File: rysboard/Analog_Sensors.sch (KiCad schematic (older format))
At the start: 25 parts, among them J14 BAT2_TH, J21 BAT3_TH, J22 BAT2_TH, J23 BAT2_TH, J8 BAT1_TH, Q10 DMP2075UFDB

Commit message: pre cleanup
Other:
- moved on the sheet: R52, R53, R55, R56, R57, TH2
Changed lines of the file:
@@
 $Descr A4 11693 8268
 encoding utf-8
-Sheet 6 7
+Sheet 5 7
 Title ""
 Date ""
@@
 Text HLabel 4100 1300 0    50   Input ~ 0
 BAT_T_3
-Text HLabel 2500 2525 0    50   Input ~ 0
+Text HLabel 3150 2875 0    50   Input ~ 0
 BOARD_T_1
 Text HLabel 6150 1275 0    50   Input ~ 0
 CHASSIS_T_2
-Text HLabel 1700 4550 0    50   Input ~ 0
+Text HLabel 2425 4375 0    50   Input ~ 0
 V_P_20
-Text HLabel 2850 4550 0    50   Input ~ 0
+Text HLabel 3575 4375 0    50   Input ~ 0
 V_P_5
 Text HLabel 1600 5650 0    50   Input ~ 0
@@
 $EndComp
 Wire Wire Line
-	2500 2175 2500 2225
+	3150 2525 3150 2575
 $Comp
 L power:GND #PWR049
 U 1 1 603EF9F9
-P 2100 2925
-F 0 "#PWR049" H 2100 2675 50  0001 C CNN
-F 1 "GND" H 2105 2752 50  0000 C CNN
-F 2 "" H 2100 2925 50  0001 C CNN
-F 3 "" H 2100 2925 50  0001 C CNN
-	1    2100 2925
+P 2750 3275
+F 0 "#PWR049" H 2750 3025 50  0001 C CNN
+F 1 "GND" H 2755 3102 50  0000 C CNN
+F 2 "" H 2750 3275 50  0001 C CNN
+F 3 "" H 2750 3275 50  0001 C CNN
+	1    2750 3275
 	-1   0    0    -1
 $EndComp
@@
 L Device:Thermistor_PTC TH2
 U 1 1 603F0105
-P 2500 2675
-F 0 "TH2" H 2598 2721 50  0000 L CNN
-F 1 "Thermistor_PTC" H 2598 2630 50  0000 L CNN
-F 2 "Resistor_SMD:R_0805_2012Metric_Pad1.15x1.40mm_HandSolder" H 2550 2475 50  0001 L CNN
-F 3 "~" H 2500 2675 50  0001 C CNN
-	1    2500 2675
-	1    0    0    -1
-$EndComp
-Wire Wire Line
-	2100 2825 2100 2925
-Wire Wire Line
-	2500 2825 2100 2825
+P 3150 3025
+F 0 "TH2" H 3248 3071 50  0000 L CNN
+F 1 "Thermistor_PTC" H 3248 2980 50  0000 L CNN
+F 2 "Resistor_SMD:R_0805_2012Metric_Pad1.15x1.40mm_HandSolder" H 3200 2825 50  0001 L CNN
+F 3 "~" H 3150 3025 50  0001 C CNN
+	1    3150 3025
+	1    0    0    -1
+$EndComp
+Wire Wire Line
+	2750 3175 2750 3275
+Wire Wire Line
+	3150 3175 2750 3175
 $Comp
 L power:+24V #PWR026
 U 1 1 603F23C7
-P 2050 4250
-F 0 "#PWR026" H 2050 4100 50  0001 C CNN
-F 1 "+24V" H 2065 4423 50  0000 C CNN
-F 2 "" H 2050 4250 50  0001 C CNN
-F 3 "" H 2050 4250 50  0001 C CNN
-	1    2050 4250
+P 2775 4075
+F 0 "#PWR026" H 2775 3925 50  0001 C CNN
+F 1 "+24V" H 2790 4248 50  0000 C CNN
+F 2 "" H 2775 4075 50  0001 C CNN
+F 3 "" H 2775 4075 50  0001 C CNN
+	1    2775 4075
 	1    0    0    -1
 $EndComp
@@
 L power:+5V #PWR051
 U 1 1 603F2BD7
-P 3150 4250
-F 0 "#PWR051" H 3150 4100 50  0001 C CNN
-F 1 "+5V" H 3165 4423 50  0000 C CNN
-F 2 "" H 3150 4250 50  0001 C CNN
-F 3 "" H 3150 4250 50  0001 C CNN
-	1    3150 4250
-	1    0    0    -1
-$EndComp
-Wire Wire Line
-	3150 4550 2850 4550
+P 3875 4075
+F 0 "#PWR051" H 3875 3925 50  0001 C CNN
+F 1 "+5V" H 3890 4248 50  0000 C CNN
+F 2 "" H 3875 4075 50  0001 C CNN
+F 3 "" H 3875 4075 50  0001 C CNN
+	1    3875 4075
+	1    0    0    -1
+$EndComp
+Wire Wire Line
+	3875 4375 3575 4375
 Text GLabel 2050 5650 2    50   Output ~ 0
 Bat_Current_Pos
@@
 L Device:R R52
 U 1 1 60405D8A
-P 2050 4400
-F 0 "R52" H 2120 4446 50  0000 L CNN
-F 1 "9KR0.5%" H 2120 4355 50  0000 L CNN
-F 2 "Resistor_SMD:R_0603_1608Metric" V 1980 4400 50  0001 C CNN
-F 3 "~" H 2050 4400 50  0001 C CNN
-	1    2050 4400
+P 2775 4225
+F 0 "R52" H 2845 4271 50  0000 L CNN
+F 1 "9KR0.5%" H 2845 4180 50  0000 L CNN
+F 2 "Resistor_SMD:R_0603_1608Metric" V 2705 4225 50  0001 C CNN
+F 3 "~" H 2775 4225 50  0001 C CNN
+	1    2775 4225
 	1    0    0    -1
 $EndComp
@@
 L Device:R R53
 U 1 1 60406110
-P 2050 4700
-F 0 "R53" H 1980 4654 50  0000 R CNN
-F 1 "1KR0.5%" H 1980 4745 50  0000 R CNN
-F 2 "Resistor_SMD:R_0603_1608Metric" V 1980 4700 50  0001 C CNN
-F 3 "~" H 2050 4700 50  0001 C CNN
-	1    2050 4700
+P 2775 4525
+F 0 "R53" H 2705 4479 50  0000 R CNN
+F 1 "1KR0.5%" H 2705 4570 50  0000 R CNN
+F 2 "Resistor_SMD:R_0603_1608Metric" V 2705 4525 50  0001 C CNN
+F 3 "~" H 2775 4525 50  0001 C CNN
+	1    2775 4525
 	-1   0    0    1
 $EndComp
@@
 L power:GND #PWR028
 U 1 1 6040647E
-P 2050 4850
-F 0 "#PWR028" H 2050 4600 50  0001 C CNN
-F 1 "GND" H 2055 4677 50  0000 C CNN
-F 2 "" H 2050 4850 50  0001 C CNN
-F 3 "" H 2050 4850 50  0001 C CNN
-	1    2050 4850
+P 2775 4675
+F 0 "#PWR028" H 2775 4425 50  0001 C CNN
+F 1 "GND" H 2780 4502 50  0000 C CNN
+F 2 "" H 2775 4675 50  0001 C CNN
+F 3 "" H 2775 4675 50  0001 C CNN
+	1    2775 4675
 	-1   0    0    -1
 $EndComp
 Wire Wire Line
-	1700 4550 2050 4550
-Connection ~ 2050 4550
+	2425 4375 2775 4375
+Connection ~ 2775 4375
 $Comp
 L power:GND #PWR052
 U 1 1 604093E1
-P 3150 4850
-F 0 "#PWR052" H 3150 4600 50  0001 C CNN
-F 1 "GND" H 3155 4677 50  0000 C CNN
-F 2 "" H 3150 4850 50  0001 C CNN
-F 3 "" H 3150 4850 50  0001 C CNN
-	1    3150 4850
+P 3875 4675
+F 0 "#PWR052" H 3875 4425 50  0001 C CNN
+F 1 "GND" H 3880 4502 50  0000 C CNN
+F 2 "" H 3875 4675 50  0001 C CNN
+F 3 "" H 3875 4675 50  0001 C CNN
+	1    3875 4675
 	-1   0    0    -1
 $EndComp
-Text Notes 3950 4850 0    50   ~ 0
+Text Notes 4675 4675 0    50   ~ 0
 33v == 3.3v\n\nR=U/I\nI=U/R1+R2\nR1 =90KOhm\nR2 = 10KOhm\n\n9.9 == 3.3V\nR1 = 10KOhm\nR2 =  5KOhm
-Text Notes 3900 3900 0    50   ~ 0
+Text Notes 4625 3725 0    50   ~ 0
 TO DO:\nDouble check values\n
 $Comp
@@
 L Device:R R56
 U 1 1 603B9257
-P 3150 4400
-F 0 "R56" H 3220 4446 50  0000 L CNN
-F 1 "10KR" H 3220 4355 50  0000 L CNN
-F 2 "Resistor_SMD:R_0603_1608Metric" V 3080 4400 50  0001 C CNN
-F 3 "~" H 3150 4400 50  0001 C CNN
-	1    3150 4400
+P 3875 4225
+F 0 "R56" H 3945 4271 50  0000 L CNN
+F 1 "10KR" H 3945 4180 50  0000 L CNN
+F 2 "Resistor_SMD:R_0603_1608Metric" V 3805 4225 50  0001 C CNN
+F 3 "~" H 3875 4225 50  0001 C CNN
+	1    3875 4225
 	1    0    0    -1
 $EndComp
@@
 L Device:R R57
 U 1 1 603B976E
-P 3150 4700
-F 0 "R57" H 3220 4746 50  0000 L CNN
-F 1 "5KR" H 3220 4655 50  0000 L CNN
-F 2 "Resistor_SMD:R_0603_1608Metric" V 3080 4700 50  0001 C CNN
-F 3 "~" H 3150 4700 50  0001 C CNN
-	1    3150 4700
-	1    0    0    -1
-$EndComp
-Connection ~ 3150 4550
+P 3875 4525
+F 0 "R57" H 3945 4571 50  0000 L CNN
+F 1 "5KR" H 3945 4480 50  0000 L CNN
+F 2 "Resistor_SMD:R_0603_1608Metric" V 3805 4525 50  0001 C CNN
+F 3 "~" H 3875 4525 50  0001 C CNN
+	1    3875 4525
+	1    0    0    -1
+$EndComp
+Connection ~ 3875 4375
 Text GLabel 8625 1800 1    50   Output ~ 0
 MCU_3.3V
@@
 L Device:R R55
 U 1 1 603BD637
-P 2500 2375
-F 0 "R55" H 2570 2421 50  0000 L CNN
-F 1 "10KR" H 2570 2330 50  0000 L CNN
-F 2 "Resistor_SMD:R_0603_1608Metric" V 2430 2375 50  0001 C CNN
-F 3 "~" H 2500 2375 50  0001 C CNN
-	1    2500 2375
+P 3150 2725
+F 0 "R55" H 3220 2771 50  0000 L CNN
+F 1 "10KR" H 3220 2680 50  0000 L CNN
+F 2 "Resistor_SMD:R_0603_1608Metric" V 3080 2725 50  0001 C CNN
+F 3 "~" H 3150 2725 50  0001 C CNN
+	1    3150 2725
 	1    0    0    -1
 $EndComp
@@
 Wire Wire Line
 	5250 750  5250 900
-Text GLabel 2500 2175 0    50   Input ~ 0
+Text GLabel 3150 2525 0    50   Input ~ 0
 MCU_ANALOG_SENSOR_V
 $EndSCHEMATC

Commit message: cleanup and energy managment scheeme started
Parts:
- removed J14: BAT2_TH, symbol Connector_Generic:Conn_01x02
- removed J21: BAT3_TH, symbol Connector_Generic:Conn_01x02
- removed J8: BAT1_TH, symbol Connector_Generic:Conn_01x02
- removed R54, R58, R60: 10KR, Resistor_SMD:R_0603_1608Metric, symbol Device:R
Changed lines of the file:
@@
 Comment4 ""
 $EndDescr
-Text HLabel 3325 1300 0    50   Input ~ 0
-BAT_T_2
-Text HLabel 4100 1300 0    50   Input ~ 0
-BAT_T_3
 Text HLabel 3150 2875 0    50   Input ~ 0
 BOARD_T_1
@@
 Text HLabel 7850 4550 0    50   Input ~ 0
 V_BAT_C3
-$Comp
-L Connector_Generic:Conn_01x02 J8
-U 1 1 603EB5C9
-P 2500 1550
-F 0 "J8" V 2372 1630 50  0000 L CNN
-F 1 "BAT1_TH" V 2463 1630 50  0000 L CNN
-F 2 "" H 2500 1550 50  0001 C CNN
-F 3 "~" H 2500 1550 50  0001 C CNN
-	1    2500 1550
-	0    1    1    0
-$EndComp
-$Comp
-L Connector_Generic:Conn_01x02 J14
-U 1 1 603EBF1A
-P 3475 1550
-F 0 "J14" V 3347 1630 50  0000 L CNN
-F 1 "BAT2_TH" V 3438 1630 50  0000 L CNN
-F 2 "" H 3475 1550 50  0001 C CNN
-F 3 "~" H 3475 1550 50  0001 C CNN
-	1    3475 1550
-	0    1    1    0
-$EndComp
-$Comp
-L Connector_Generic:Conn_01x02 J21
-U 1 1 603EC2EC
-P 4250 1550
-F 0 "J21" V 4122 1630 50  0000 L CNN
-F 1 "BAT3_TH" V 4213 1630 50  0000 L CNN
-F 2 "" H 4250 1550 50  0001 C CNN
-F 3 "~" H 4250 1550 50  0001 C CNN
-	1    4250 1550
-	0    1    1    0
-$EndComp
-$Comp
-L power:GND #PWR050
-U 1 1 603ED9D9
-P 2500 1350
-F 0 "#PWR050" H 2500 1100 50  0001 C CNN
-F 1 "GND" H 2505 1177 50  0000 C CNN
-F 2 "" H 2500 1350 50  0001 C CNN
-F 3 "" H 2500 1350 50  0001 C CNN
-	1    2500 1350
-	0    -1   1    0
-$EndComp
-$Comp
-L power:GND #PWR053
-U 1 1 603EDE43
-P 3475 1350
-F 0 "#PWR053" H 3475 1100 50  0001 C CNN
-F 1 "GND" H 3480 1177 50  0000 C CNN
-F 2 "" H 3475 1350 50  0001 C CNN
-F 3 "" H 3475 1350 50  0001 C CNN
-	1    3475 1350
-	0    -1   -1   0
-$EndComp
-$Comp
-L power:GND #PWR054
-U 1 1 603EE031
-P 4250 1350
-F 0 "#PWR054" H 4250 1100 50  0001 C CNN
-F 1 "GND" H 4255 1177 50  0000 C CNN
-F 2 "" H 4250 1350 50  0001 C CNN
-F 3 "" H 4250 1350 50  0001 C CNN
-	1    4250 1350
-	0    -1   -1   0
-$EndComp
 Wire Wire Line
 	3150 2525 3150 2575
@@
 Text Notes 7750 3650 0    50   ~ 0
 0-15.086V\n
-Text HLabel 2350 1300 0    50   Input ~ 0
-BAT_T_1
-Wire Wire Line
-	2350 1300 2400 1300
-Wire Wire Line
-	2400 1300 2400 1350
-Wire Wire Line
-	2400 1300 2400 1250
-Connection ~ 2400 1300
-Wire Wire Line
-	3325 1300 3375 1300
-Wire Wire Line
-	3375 1300 3375 1250
-Wire Wire Line
-	3375 1300 3375 1350
-Connection ~ 3375 1300
-Wire Wire Line
-	4100 1300 4150 1300
-Wire Wire Line
-	4150 1300 4150 1250
-Wire Wire Line
-	4150 1300 4150 1350
-Connection ~ 4150 1300
 $Comp
 L Device:R R70
@@
 Text GLabel 8625 1800 1    50   Output ~ 0
 MCU_3.3V
-Wire Wire Line
-	2400 900  2400 950
-Wire Wire Line
-	4150 900  4150 950
 $Comp
 L Device:R R55
@@
 When not used, thermistors do not need to be powered on.
 $Comp
-L Device:R R54
-U 1 1 603FD549
-P 2400 1100
-F 0 "R54" H 2470 1146 50  0000 L CNN
-F 1 "10KR" H 2470 1055 50  0000 L CNN
-F 2 "Resistor_SMD:R_0603_1608Metric" V 2330 1100 50  0001 C CNN
-F 3 "~" H 2400 1100 50  0001 C CNN
-	1    2400 1100
-	1    0    0    -1
-$EndComp
-$Comp
-L Device:R R58
-U 1 1 603FD808
-P 3375 1100
-F 0 "R58" H 3445 1146 50  0000 L CNN
-F 1 "10KR" H 3445 1055 50  0000 L CNN
-F 2 "Resistor_SMD:R_0603_1608Metric" V 3305 1100 50  0001 C CNN
-F 3 "~" H 3375 1100 50  0001 C CNN
-	1    3375 1100
-	1    0    0    -1
-$EndComp
-$Comp
-L Device:R R60
-U 1 1 603FDA2E
-P 4150 1100
-F 0 "R60" H 4220 1146 50  0000 L CNN
-F 1 "10KR" H 4220 1055 50  0000 L CNN
-F 2 "Resistor_SMD:R_0603_1608Metric" V 4080 1100 50  0001 C CNN
-F 3 "~" H 4150 1100 50  0001 C CNN
-	1    4150 1100
-	1    0    0    -1
-$EndComp
-$Comp
 L rysboard:DMP2075UFDB Q10
 U 1 1 605EDFDE
@@
 Wire Wire Line
 	6150 1225 6150 1375
-Text HLabel 5250 1275 0    50   Input ~ 0
-CHASSIS_T_1
 Wire Wire Line
 	5250 1200 5250 1350
@@
 Text GLabel 5250 750  2    50   Input ~ 0
 MCU_ANALOG_SENSOR_V
-Text GLabel 4150 900  2    50   Input ~ 0
-MCU_ANALOG_SENSOR_V
-Text GLabel 3375 750  2    50   Input ~ 0
-MCU_ANALOG_SENSOR_V
-Wire Wire Line
-	3375 750  3375 950
-Text GLabel 2400 900  2    50   Input ~ 0
-MCU_ANALOG_SENSOR_V
 Wire Wire Line
 	5250 750  5250 900
 Text GLabel 3150 2525 0    50   Input ~ 0
 MCU_ANALOG_SENSOR_V
+Text HLabel 5250 1275 0    50   Input ~ 0
+CHASSIS_T_1
 $EndSCHEMATC

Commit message: started board project
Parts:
- J22: value BAT2_TH -> CH1_T; footprint (none) -> Connector_PinHeader_2.54mm:PinHeader_1x02_P2.54mm_Vertical
- J23: value BAT2_TH -> CH2_T; footprint (none) -> Connector_PinHeader_2.54mm:PinHeader_1x02_P2.54mm_Vertical
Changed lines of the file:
@@
 P 6250 1575
 F 0 "J23" V 6122 1655 50  0000 L CNN
-F 1 "BAT2_TH" V 6213 1655 50  0000 L CNN
-F 2 "" H 6250 1575 50  0001 C CNN
+F 1 "CH2_T" V 6213 1655 50  0000 L CNN
+F 2 "Connector_PinHeader_2.54mm:PinHeader_1x02_P2.54mm_Vertical" H 6250 1575 50  0001 C CNN
 F 3 "~" H 6250 1575 50  0001 C CNN
 	1    6250 1575
@@
 P 5350 1550
 F 0 "J22" V 5222 1630 50  0000 L CNN
-F 1 "BAT2_TH" V 5313 1630 50  0000 L CNN
-F 2 "" H 5350 1550 50  0001 C CNN
+F 1 "CH1_T" V 5313 1630 50  0000 L CNN
+F 2 "Connector_PinHeader_2.54mm:PinHeader_1x02_P2.54mm_Vertical" H 5350 1550 50  0001 C CNN
 F 3 "~" H 5350 1550 50  0001 C CNN
 	1    5350 1550

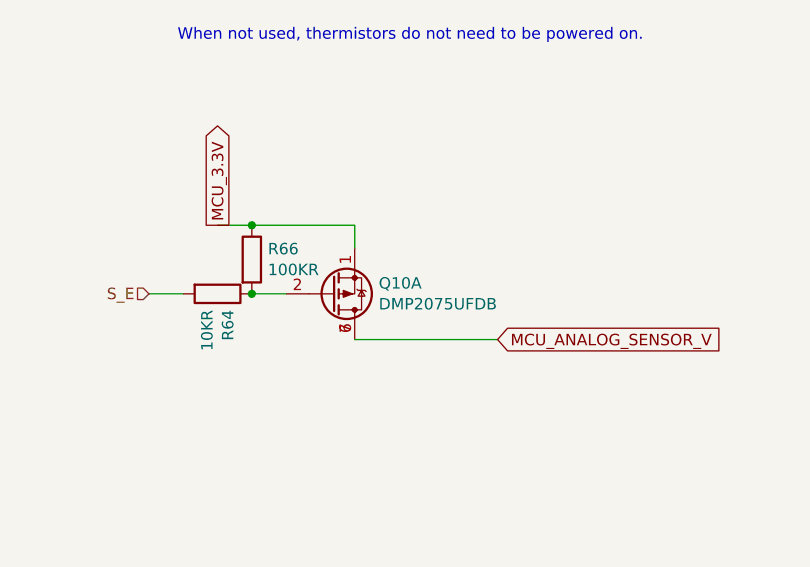
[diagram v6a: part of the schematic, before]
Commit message: st motor drivers done
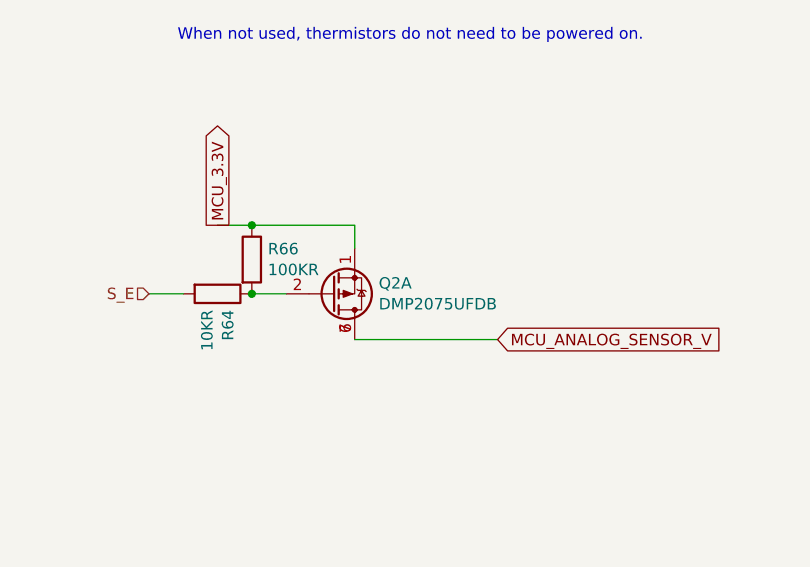
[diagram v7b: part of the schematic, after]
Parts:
- renumbered Q10 to Q2
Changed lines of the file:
@@
 When not used, thermistors do not need to be powered on.
 $Comp
-L rysboard:DMP2075UFDB Q10
+L rysboard:DMP2075UFDB Q2
 U 1 1 605EDFDE
 P 9125 2100
-F 0 "Q10" H 9330 2054 50  0000 L CNN
+F 0 "Q2" H 9330 2054 50  0000 L CNN
 F 1 "DMP2075UFDB" H 9330 2145 50  0000 L CNN
 F 2 "SamacSys_Parts:DMP2075UFDB7" H 9325 2025 50  0001 L CIN

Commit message: stm scheeme
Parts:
- added R?: 10KR, Resistor_SMD:R_0603_1608Metric, symbol Device:R
- added TH?: Thermistor_PTC, Resistor_SMD:R_0805_2012Metric_Pad1.15x1.40mm_HandSolder, symbol Device:Thermistor_PTC
- J22, J23: footprint Connector_PinHeader_2.54mm:PinHeader_1x02_P2.54mm_Vertical -> Connector_PinHeader_1.00mm:PinHeader_1x02_P1.00mm_Vertical
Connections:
- net GND: now also TH?.2
- net MCU_ANALOG_SENSOR_V: now also R?.1
- new net: R?.2, TH?.1
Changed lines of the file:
@@
 0-15.086V\n
-$Comp
-L Device:R R70
-U 1 1 603B8902
-P 7050 4400
-F 0 "R70" H 7120 4446 50  0000 L CNN
-F 1 "10KR" H 7120 4355 50  0000 L CNN
-F 2 "Resistor_SMD:R_0603_1608Metric" V 6980 4400 50  0001 C CNN
-F 3 "~" H 7050 4400 50  0001 C CNN
-	1    7050 4400
-	1    0    0    -1
-$EndComp
 $Comp
 L Device:R R71
@@
 F 0 "J23" V 6122 1655 50  0000 L CNN
 F 1 "CH2_T" V 6213 1655 50  0000 L CNN
-F 2 "Connector_PinHeader_2.54mm:PinHeader_1x02_P2.54mm_Vertical" H 6250 1575 50  0001 C CNN
+F 2 "Connector_PinHeader_1.00mm:PinHeader_1x02_P1.00mm_Vertical" H 6250 1575 50  0001 C CNN
 F 3 "~" H 6250 1575 50  0001 C CNN
 	1    6250 1575
@@
 F 0 "J22" V 5222 1630 50  0000 L CNN
 F 1 "CH1_T" V 5313 1630 50  0000 L CNN
-F 2 "Connector_PinHeader_2.54mm:PinHeader_1x02_P2.54mm_Vertical" H 5350 1550 50  0001 C CNN
+F 2 "Connector_PinHeader_1.00mm:PinHeader_1x02_P1.00mm_Vertical" H 5350 1550 50  0001 C CNN
 F 3 "~" H 5350 1550 50  0001 C CNN
 	1    5350 1550
@@
 Text HLabel 5250 1275 0    50   Input ~ 0
 CHASSIS_T_1
+$Comp
+L Device:R R70
+U 1 1 603B8902
+P 7050 4400
+F 0 "R70" H 7120 4446 50  0000 L CNN
+F 1 "10KR" H 7120 4355 50  0000 L CNN
+F 2 "Resistor_SMD:R_0603_1608Metric" V 6980 4400 50  0001 C CNN
+F 3 "~" H 7050 4400 50  0001 C CNN
+	1    7050 4400
+	1    0    0    -1
+$EndComp
+$Comp
+L Device:Thermistor_PTC TH?
+U 1 1 6063752B
+P 3975 3025
+F 0 "TH?" H 4073 3071 50  0000 L CNN
+F 1 "Thermistor_PTC" H 4073 2980 50  0000 L CNN
+F 2 "Resistor_SMD:R_0805_2012Metric_Pad1.15x1.40mm_HandSolder" H 4025 2825 50  0001 L CNN
+F 3 "~" H 3975 3025 50  0001 C CNN
+	1    3975 3025
+	1    0    0    -1
+$EndComp
+Wire Wire Line
+	3975 3175 3150 3175
+Connection ~ 3150 3175
+$Comp
+L Device:R R?
+U 1 1 6063841E
+P 3975 2700
+F 0 "R?" H 4045 2746 50  0000 L CNN
+F 1 "10KR" H 4045 2655 50  0000 L CNN
+F 2 "Resistor_SMD:R_0603_1608Metric" V 3905 2700 50  0001 C CNN
+F 3 "~" H 3975 2700 50  0001 C CNN
+	1    3975 2700
+	1    0    0    -1
+$EndComp
+Wire Wire Line
+	3150 2525 3975 2525
+Wire Wire Line
+	3975 2525 3975 2550
+Wire Wire Line
+	3975 2875 3975 2850
 $EndSCHEMATC
